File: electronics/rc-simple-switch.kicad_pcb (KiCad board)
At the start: 2 copper layers, 17 x 8 mm, 13 parts, among them K1 CONN_3, K2 CONN_3, P1 CONN_1, P2 CONN_1, P3 CONN_1, P4 CONN_1, P5 CONN_1, Q1 PMV30UN, U1 PIC10F200

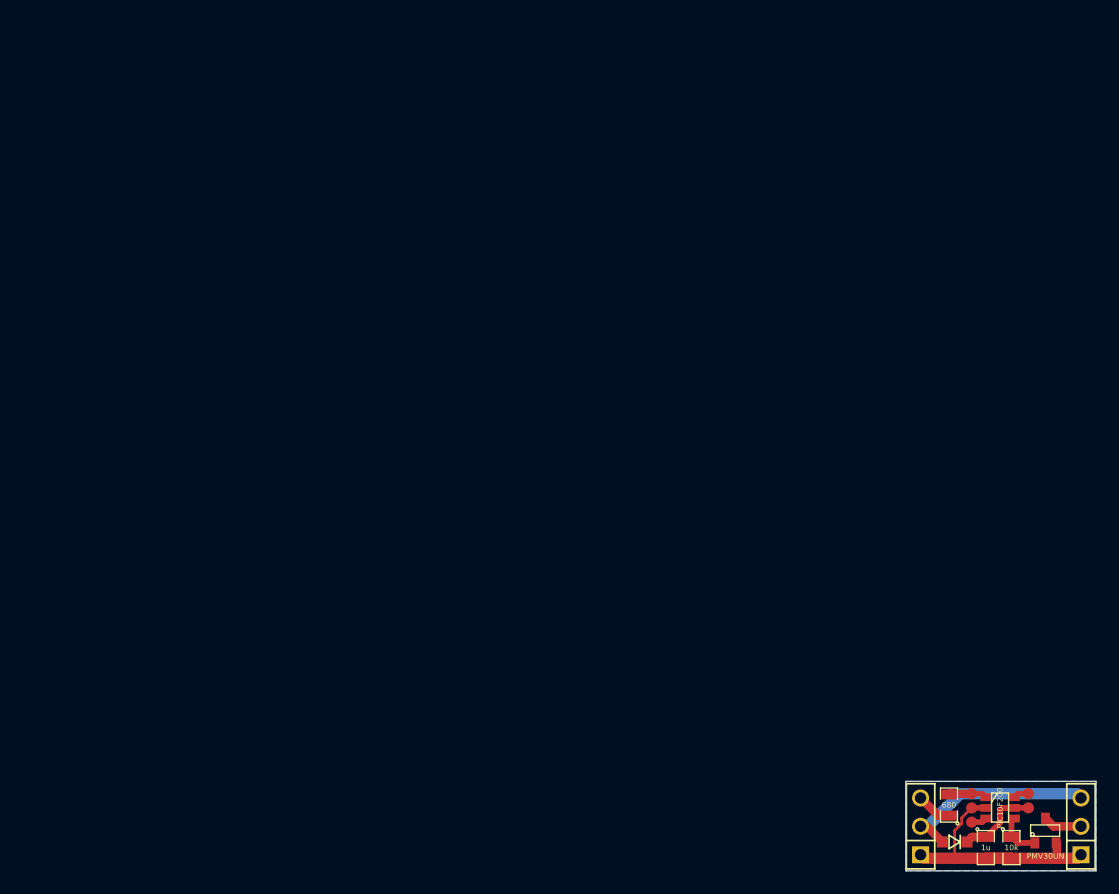
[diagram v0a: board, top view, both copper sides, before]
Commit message: Re-design layout and move to latest Kicad version
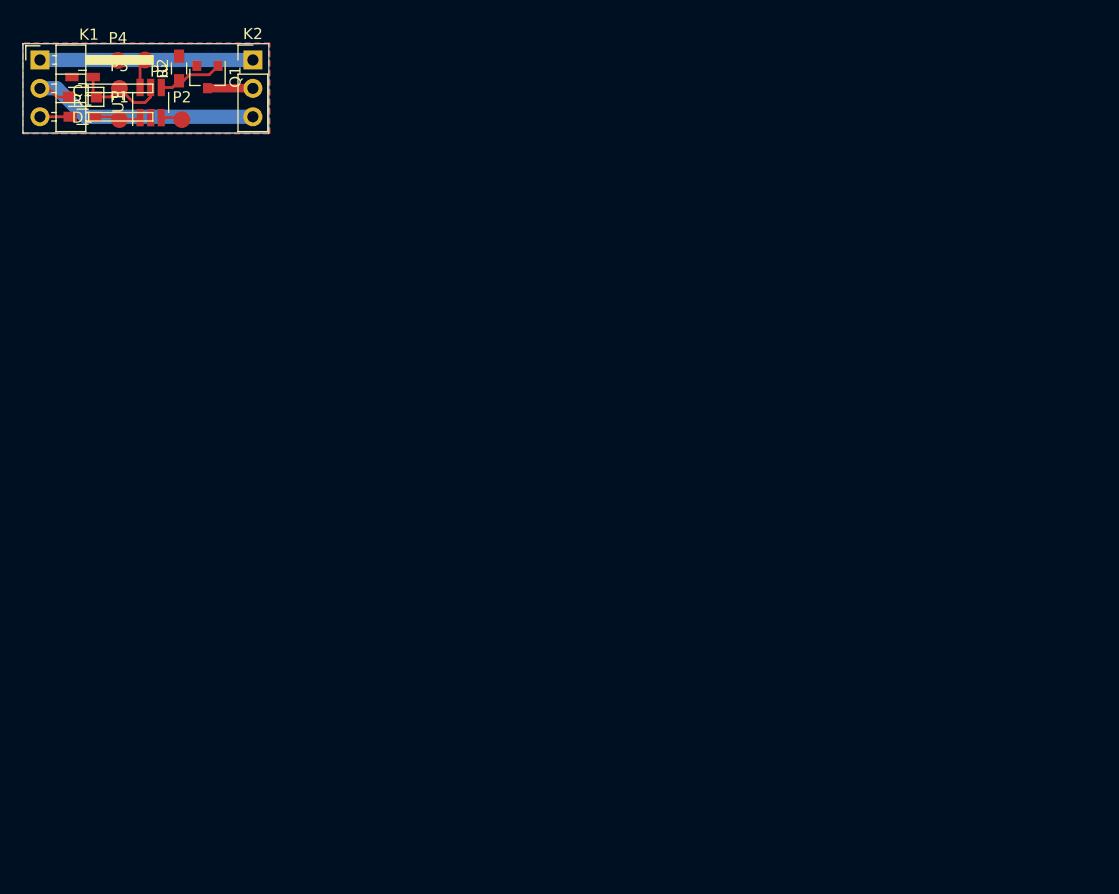
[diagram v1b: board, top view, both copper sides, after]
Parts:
- C1: footprint SM0805 -> Capacitors_SMD:C_0603_HandSoldering
- D1: footprint SOD323 -> Diodes_SMD:D_SOD-323_HandSoldering
- K1: footprint PIN_ARRAY_3X1 -> Pin_Headers:Pin_Header_Angled_1x03_Pitch2.54mm
- K2: footprint PIN_ARRAY_3X1 -> Pin_Headers:Pin_Header_Straight_1x03_Pitch2.54mm
- P1, P2, P3, P4, P5: footprint Test_pad_1mm -> Measurement_Points:Measurement_Point_Round-SMD-Pad_Small
- Q1: footprint SOT23 -> TO_SOT_Packages_SMD:SOT-23
- R1, R2: footprint SM0805 -> Resistors_SMD:R_0603_HandSoldering
- U1: footprint SOT23_6 -> TO_SOT_Packages_SMD:SOT-23-6_Handsoldering
- moved C1 106.2 mm to (105.3, 99.0), turned to 180 degrees
- moved K1 104.4 mm to (101.5, 97.5), turned to 0 degrees
- moved P5 103.7 mm to (108.6, 100.0)
- moved P3 102.7 mm to (110.9, 97.5)
- moved D1 102.6 mm to (105.3, 100.8), turned to 180 degrees
- moved R2 102.0 mm to (114.0, 98.2), turned to 90 degrees
- moved P4 101.5 mm to (108.5, 97.5)
- moved K2 100.9 mm to (120.6, 97.5), turned to 0 degrees
- moved Q1 100.8 mm to (116.5, 99.0), turned to 270 degrees
- moved R1 99.0 mm to (105.3, 102.5), turned to 0 degrees
- moved U1 98.8 mm to (111.4, 101.3), turned to 90 degrees
- moved P1 97.2 mm to (108.6, 102.8)
- moved P2 94.6 mm to (114.2, 102.8)
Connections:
- net VSS renamed GND
- D1 pad 1: VCC -> VDD
- D1 pad 2: VDD -> VCC
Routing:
- net GND: track 24.7 -> 19.0 mm
- net VCC: track 18.2 -> 23.0 mm
- net /OUT: track 4.07 -> 6.18 mm
- net VDD: track 7.40 -> 8.64 mm
- net Net-(P3-Pad1): track 1.40 -> 2.64 mm
- net Net-(P1-Pad1): track 3.46 -> 4.22 mm
- net Net-(K2-Pad2): track 3.47 -> 4.07 mm
- net Net-(P2-Pad1): track 1.40 -> 1.92 mm
- added copper zone on F.Cu, net GND
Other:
- board size 17 x 8 mm -> 22 x 8 mm
- net class Default: clearance 0.1524 -> 0.2032; via_dia 0.889 -> 0.6; via_drill 0.635 -> 0.4
- net class Power removed
- rule trace_clearance: 0.1524 -> 0.2032
- rule trace_min: 0.254 -> 0.2032
- rule via_min_drill: 0.508 -> 0.3
- rule via_min_size: 0.889 -> 0.4
- board text removed: "+"
- board text removed: "-"
- board text removed: "LANE Boys RC"
- board text removed: "RC on/off switch"
- board text removed: "S"

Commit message: Finish PCB re-layout
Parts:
- K1, K2: moved to B.Cu
- R1: value 680 -> 1k
- moved P5 3.86 mm to (107.0, 96.5)
- moved P2 3.30 mm to (111.0, 103.5)
- moved Q1 2.71 mm to (114.0, 100.0), turned to 0 degrees
- moved P4 2.69 mm to (111.0, 96.5)
- moved K2 2.54 mm to (118.0, 97.5), turned to 180 degrees
- moved U1 2.18 mm to (109.7, 100.0)
- moved P3 2.15 mm to (109.0, 96.5)
- moved R2 0.90 mm to (114.1, 97.3), turned to 0 degrees
- moved P1 0.79 mm to (109.0, 103.5)
- moved R1 0.76 mm to (105.3, 103.3)
- moved C1 0.51 mm to (105.3, 98.5)
- turned K1 to 180 degrees
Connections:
- net Net-(K1-Pad3) renamed /S
- net Net-(K2-Pad2) renamed /SW
- net Net-(P1-Pad1) renamed /DAT
- net Net-(P2-Pad1) renamed /CLK
- net Net-(P3-Pad1) renamed /VPP
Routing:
- net GND: track 19.0 -> 0.00 mm
- net /OUT: track 6.18 -> 4.28 mm
- net /SW: track 4.07 -> 3.03 mm
- net /DAT: track 4.22 -> 5.20 mm
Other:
- board size 22 x 8 mm -> 20 x 10 mm
- board text added: "+"
- board text added: "-"
- board text added: "LANE Boys RC"
- board text added: "RC switch"
- board text added: "S"
- board text added: "SW"

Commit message: Add PCB revision
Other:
- board text added: "Rev 2"
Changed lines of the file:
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@@
     (area 99.949999 94.949999 120.050001 105.050001)
     (thickness 1.6)
-    (drawings 22)
+    (drawings 23)
     (tracks 32)
     (zones 0)
@@
   )
   (setup
-    (last_trace_width 0.508)
+    (last_trace_width 0.254)
     (user_trace_width 0.381)
     (user_trace_width 0.508)
@@
       (net 2 GND))
   )
+  (gr_text "Rev 2" (at 114.478 103.556) (layer F.SilkS)
+    (effects (font (size 1 1) (thickness 0.15)))
+  )
   (gr_text "RC switch" (at 110.16 96.19 180) (layer B.SilkS)
